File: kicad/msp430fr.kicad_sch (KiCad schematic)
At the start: 14 parts, among them U1006 MSP430FR5994IZVW, Y1003 Crystal

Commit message: unify module and board
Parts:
- renumbered C1029 to C61, C1030 to C62, C1031 to C63, C1032 to C64, C1033 to C65, C1034 to C66, C1035 to C67, C1036 to C68, C1037 to C69, C1038 to C70, C1039 to C71, R1021 to R54, U1006 to U16, Y1003 to Y5

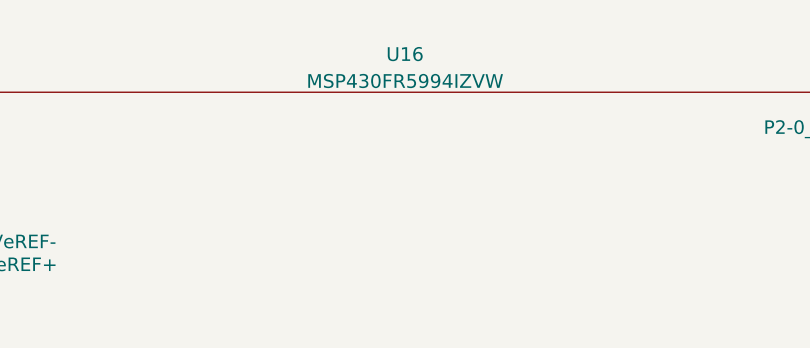
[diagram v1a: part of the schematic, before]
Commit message: move module parts to common library
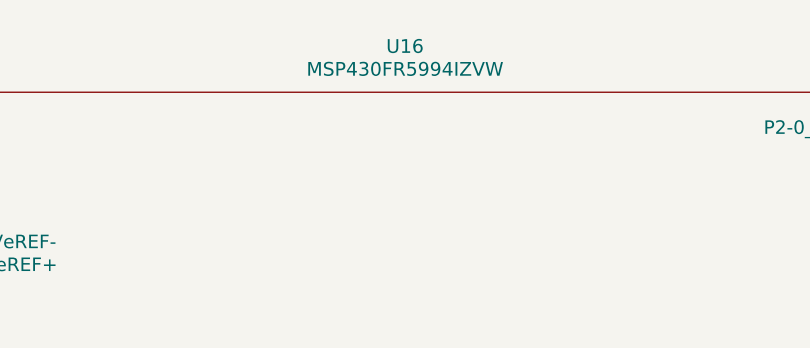
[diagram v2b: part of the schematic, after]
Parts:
- U16: symbol Riotee:MSP430FR5994IZVW -> riotee:MSP430FR5994IZVW
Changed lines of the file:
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@@
 	)
 	(symbol
-		(lib_id "Riotee:MSP430FR5994IZVW")
+		(lib_id "riotee:MSP430FR5994IZVW")
 		(at 146.05 97.79 0)
 		(unit 1)
@@
 		(fields_autoplaced yes)
 		(property "Reference" "U16"
-			(at 146.05 19.9443 0)
+			(at 146.05 19.05 0)
 			(effects
 				(font
@@
 		)
 		(property "Value" "MSP430FR5994IZVW"
-			(at 146.05 22.9377 0)
+			(at 146.05 21.59 0)
 			(effects
 				(font
@@
 		)
 		(property "Footprint" "Riotee:TI_ZVW"
-			(at 148.59 178.054 0)
+			(at 146.05 155.194 0)
 			(effects
 				(font
@@
 		)
 		(property "Datasheet" ""
-			(at 148.59 176.53 0)
+			(at 146.05 153.67 0)
 			(effects
 				(font

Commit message: resolve ERC
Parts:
- C61, C62, C63, C64, C65, C66, C67, C68, C69, C70, C71: footprint Riotee:C_0201_0603Metric -> riotee:C_0201_0603Metric; symbol Riotee:C -> Device:C
- R54: footprint Riotee:R_0201_0603Metric -> riotee:R_0201_0603Metric; symbol Riotee:R -> Device:R
- U16: footprint Riotee:TI_ZVW -> riotee:TI_ZVW
- Y5: footprint Riotee:ECX-12R -> riotee:ECX-12R
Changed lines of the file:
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@@
 	)
 	(symbol
-		(lib_id "Riotee:C")
+		(lib_id "Device:C")
 		(at 88.9 175.26 0)
 		(unit 1)
@@
 			)
 		)
-		(property "Footprint" "Riotee:C_0201_0603Metric"
+		(property "Footprint" "riotee:C_0201_0603Metric"
 			(at 89.8652 179.07 0)
 			(effects
@@
 			)
 		)
-		(property "Description" "CAP CER 1UF 16V X5R 0201"
+		(property "Description" "Unpolarized capacitor"
 			(at 88.9 175.26 0)
 			(effects
@@
 	)
 	(symbol
-		(lib_id "Riotee:C")
+		(lib_id "Device:C")
 		(at 110.49 175.26 0)
 		(unit 1)
@@
 			)
 		)
-		(property "Footprint" "Riotee:C_0201_0603Metric"
+		(property "Footprint" "riotee:C_0201_0603Metric"
 			(at 111.4552 179.07 0)
 			(effects
@@
 			)
 		)
-		(property "Description" "CAP CER 1UF 16V X5R 0201"
+		(property "Description" "Unpolarized capacitor"
 			(at 110.49 175.26 0)
 			(effects
@@
 	)
 	(symbol
-		(lib_id "Riotee:C")
+		(lib_id "Device:C")
 		(at 252.73 123.19 90)
 		(unit 1)
@@
 			)
 		)
-		(property "Footprint" "Riotee:C_0201_0603Metric"
+		(property "Footprint" "riotee:C_0201_0603Metric"
 			(at 256.54 122.2248 0)
 			(effects
@@
 			)
 		)
-		(property "Description" "CAP CER 12PF 50V C0G/NP0 0201"
+		(property "Description" "Unpolarized capacitor"
 			(at 252.73 123.19 0)
 			(effects
@@
 	)
 	(symbol
-		(lib_id "Riotee:GND")
+		(lib_id "power:GND")
 		(at 134.62 186.69 0)
 		(unit 1)
@@
 			)
 		)
-		(property "Description" ""
+		(property "Description" "Power symbol creates a global label with name \"GND\" , ground"
 			(at 134.62 186.69 0)
 			(effects
@@
 	)
 	(symbol
-		(lib_id "Riotee:C")
+		(lib_id "Device:C")
 		(at 97.79 175.26 0)
 		(unit 1)
@@
 			)
 		)
-		(property "Footprint" "Riotee:C_0201_0603Metric"
+		(property "Footprint" "riotee:C_0201_0603Metric"
 			(at 98.7552 179.07 0)
 			(effects
@@
 			)
 		)
-		(property "Description" "CAP CER 0.1UF 10V X5R 0201"
+		(property "Description" "Unpolarized capacitor"
 			(at 97.79 175.26 0)
 			(effects
@@
 	)
 	(symbol
-		(lib_id "Riotee:C")
+		(lib_id "Device:C")
 		(at 43.18 175.26 0)
 		(unit 1)
@@
 			)
 		)
-		(property "Footprint" "Riotee:C_0201_0603Metric"
+		(property "Footprint" "riotee:C_0201_0603Metric"
 			(at 44.1452 179.07 0)
 			(effects
@@
 			)
 		)
-		(property "Description" "CAP CER 1UF 16V X5R 0201"
+		(property "Description" "Unpolarized capacitor"
 			(at 43.18 175.26 0)
 			(effects
@@
 	)
 	(symbol
-		(lib_id "Riotee:GND")
+		(lib_id "power:GND")
 		(at 82.55 185.42 0)
 		(unit 1)
@@
 			)
 		)
-		(property "Description" ""
+		(property "Description" "Power symbol creates a global label with name \"GND\" , ground"
 			(at 82.55 185.42 0)
 			(effects
@@
 	)
 	(symbol
-		(lib_id "Riotee:C")
+		(lib_id "Device:C")
 		(at 30.48 175.26 0)
 		(unit 1)
@@
 			)
 		)
-		(property "Footprint" "Riotee:C_0201_0603Metric"
+		(property "Footprint" "riotee:C_0201_0603Metric"
 			(at 31.4452 179.07 0)
 			(effects
@@
 			)
 		)
-		(property "Description" "CAP CER 0.1UF 10V X5R 0201"
+		(property "Description" "Unpolarized capacitor"
 			(at 30.48 175.26 0)
 			(effects
@@
 			)
 		)
-		(property "Footprint" "Riotee:TI_ZVW"
+		(property "Footprint" "riotee:TI_ZVW"
 			(at 146.05 155.194 0)
 			(effects
@@
 	)
 	(symbol
-		(lib_id "Riotee:C")
+		(lib_id "Device:C")
 		(at 53.34 175.26 0)
 		(unit 1)
@@
 			)
 		)
-		(property "Footprint" "Riotee:C_0201_0603Metric"
+		(property "Footprint" "riotee:C_0201_0603Metric"
 			(at 54.3052 179.07 0)
 			(effects
@@
 			)
 		)
-		(property "Description" "CAP CER 0.1UF 10V X5R 0201"
+		(property "Description" "Unpolarized capacitor"
 			(at 53.34 175.26 0)
 			(effects
@@
 	)
 	(symbol
-		(lib_id "Riotee:C")
+		(lib_id "Device:C")
 		(at 76.2 175.26 0)
 		(unit 1)
@@
 			)
 		)
-		(property "Footprint" "Riotee:C_0201_0603Metric"
+		(property "Footprint" "riotee:C_0201_0603Metric"
 			(at 77.1652 179.07 0)
 			(effects
@@
 			)
 		)
-		(property "Description" "CAP CER 0.1UF 10V X5R 0201"
+		(property "Description" "Unpolarized capacitor"
 			(at 76.2 175.26 0)
 			(effects
@@
 	)
 	(symbol
-		(lib_id "Riotee:GND")
+		(lib_id "power:GND")
 		(at 59.69 185.42 0)
 		(unit 1)
@@
 			)
 		)
-		(property "Description" ""
+		(property "Description" "Power symbol creates a global label with name \"GND\" , ground"
 			(at 59.69 185.42 0)
 			(effects
@@
 	)
 	(symbol
-		(lib_id "Riotee:C")
+		(lib_id "Device:C")
 		(at 252.73 135.89 90)
 		(unit 1)
@@
 			)
 		)
-		(property "Footprint" "Riotee:C_0201_0603Metric"
+		(property "Footprint" "riotee:C_0201_0603Metric"
 			(at 256.54 134.9248 0)
 			(effects
@@
 			)
 		)
-		(property "Description" "CAP CER 12PF 50V C0G/NP0 0201"
+		(property "Description" "Unpolarized capacitor"
 			(at 252.73 135.89 0)
 			(effects
@@
 	)
 	(symbol
-		(lib_id "Riotee:R")
+		(lib_id "Device:R")
 		(at 134.62 170.18 0)
 		(unit 1)
@@
 			)
 		)
-		(property "Footprint" "Riotee:R_0201_0603Metric"
+		(property "Footprint" "riotee:R_0201_0603Metric"
 			(at 132.842 170.18 90)
 			(effects
@@
 			)
 		)
-		(property "Description" "RES 47K OHM 1% 1/20W 0201"
+		(property "Description" "Resistor"
 			(at 134.62 170.18 0)
 			(effects
@@
 			)
 		)
-		(property "Footprint" "Riotee:ECX-12R"
+		(property "Footprint" "riotee:ECX-12R"
 			(at 243.84 129.54 0)
 			(effects
@@
 	)
 	(symbol
-		(lib_id "Riotee:C")
+		(lib_id "Device:C")
 		(at 66.04 175.26 0)
 		(unit 1)
@@
 			)
 		)
-		(property "Footprint" "Riotee:C_0201_0603Metric"
+		(property "Footprint" "riotee:C_0201_0603Metric"
 			(at 67.0052 179.07 0)
 			(effects
@@
 			)
 		)
-		(property "Description" "CAP CER 1UF 16V X5R 0201"
+		(property "Description" "Unpolarized capacitor"
 			(at 66.04 175.26 0)
 			(effects
@@
 	)
 	(symbol
-		(lib_id "Riotee:GND")
+		(lib_id "power:GND")
 		(at 36.83 185.42 0)
 		(unit 1)
@@
 			)
 		)
-		(property "Description" ""
+		(property "Description" "Power symbol creates a global label with name \"GND\" , ground"
 			(at 36.83 185.42 0)
 			(effects
@@
 	)
 	(symbol
-		(lib_id "Riotee:C")
+		(lib_id "Device:C")
 		(at 134.62 180.34 0)
 		(unit 1)
@@
 			)
 		)
-		(property "Footprint" "Riotee:C_0201_0603Metric"
+		(property "Footprint" "riotee:C_0201_0603Metric"
 			(at 135.5852 184.15 0)
 			(effects
@@
 			)
 		)
-		(property "Description" "CAP CER 820PF 50V C0G/NP0 0201"
+		(property "Description" "Unpolarized capacitor"
 			(at 134.62 180.34 0)
 			(effects
@@
 	)
 	(symbol
-		(lib_id "Riotee:GND")
+		(lib_id "power:GND")
 		(at 104.14 185.42 0)
 		(unit 1)
@@
 			)
 		)
-		(property "Description" ""
+		(property "Description" "Power symbol creates a global label with name \"GND\" , ground"
 			(at 104.14 185.42 0)
 			(effects

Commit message: resolve remaining import errors
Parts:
- C61, C62, C63, C64, C65, C66, C67, C68, C69, C70, C71: footprint riotee:C_0201_0603Metric -> Capacitor_SMD:C_0201_0603Metric
- R54: footprint riotee:R_0201_0603Metric -> Resistor_SMD:R_0201_0603Metric
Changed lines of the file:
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@@
 			)
 		)
-		(property "Footprint" "riotee:C_0201_0603Metric"
+		(property "Footprint" "Capacitor_SMD:C_0201_0603Metric"
 			(at 89.8652 179.07 0)
 			(effects
@@
 			)
 		)
-		(property "Footprint" "riotee:C_0201_0603Metric"
+		(property "Footprint" "Capacitor_SMD:C_0201_0603Metric"
 			(at 111.4552 179.07 0)
 			(effects
@@
 			)
 		)
-		(property "Footprint" "riotee:C_0201_0603Metric"
+		(property "Footprint" "Capacitor_SMD:C_0201_0603Metric"
 			(at 256.54 122.2248 0)
 			(effects
@@
 			)
 		)
-		(property "Footprint" "riotee:C_0201_0603Metric"
+		(property "Footprint" "Capacitor_SMD:C_0201_0603Metric"
 			(at 98.7552 179.07 0)
 			(effects
@@
 			)
 		)
-		(property "Footprint" "riotee:C_0201_0603Metric"
+		(property "Footprint" "Capacitor_SMD:C_0201_0603Metric"
 			(at 44.1452 179.07 0)
 			(effects
@@
 			)
 		)
-		(property "Footprint" "riotee:C_0201_0603Metric"
+		(property "Footprint" "Capacitor_SMD:C_0201_0603Metric"
 			(at 31.4452 179.07 0)
 			(effects
@@
 			)
 		)
-		(property "Footprint" "riotee:C_0201_0603Metric"
+		(property "Footprint" "Capacitor_SMD:C_0201_0603Metric"
 			(at 54.3052 179.07 0)
 			(effects
@@
 			)
 		)
-		(property "Footprint" "riotee:C_0201_0603Metric"
+		(property "Footprint" "Capacitor_SMD:C_0201_0603Metric"
 			(at 77.1652 179.07 0)
 			(effects
@@
 			)
 		)
-		(property "Footprint" "riotee:C_0201_0603Metric"
+		(property "Footprint" "Capacitor_SMD:C_0201_0603Metric"
 			(at 256.54 134.9248 0)
 			(effects
@@
 			)
 		)
-		(property "Footprint" "riotee:R_0201_0603Metric"
+		(property "Footprint" "Resistor_SMD:R_0201_0603Metric"
 			(at 132.842 170.18 90)
 			(effects
@@
 			)
 		)
-		(property "Footprint" "riotee:C_0201_0603Metric"
+		(property "Footprint" "Capacitor_SMD:C_0201_0603Metric"
 			(at 67.0052 179.07 0)
 			(effects
@@
 			)
 		)
-		(property "Footprint" "riotee:C_0201_0603Metric"
+		(property "Footprint" "Capacitor_SMD:C_0201_0603Metric"
 			(at 135.5852 184.15 0)
 			(effects
